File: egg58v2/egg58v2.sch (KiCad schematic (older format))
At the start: 32 parts, among them J1 AudioJack4, SW11 SW_PUSH_LED, SW12 SW_PUSH_LED, SW13 SW_PUSH_LED, SW14 SW_PUSH_LED, SW15 SW_PUSH_LED, SW16 SW_PUSH_LED, SW21 SW_PUSH_LED, SW22 SW_PUSH_LED, SW23 SW_PUSH_LED, SW24 SW_PUSH_LED, SW25 SW_PUSH_LED, SW26 SW_PUSH_LED, SW31 SW_PUSH_LED, SW32 SW_PUSH_LED, SW33 SW_PUSH_LED, SW34 SW_PUSH_LED, SW35 SW_PUSH_LED, SW36 SW_PUSH_LED, SW41 SW_PUSH_LED, SW42 SW_PUSH_LED, SW43 SW_PUSH_LED, SW44 SW_PUSH_LED, SW45 SW_PUSH_LED, SW46 SW_PUSH_LED, SW52 SW_PUSH_LED, SW53 SW_PUSH_LED, SW54 SW_PUSH_LED, SW55 SW_PUSH_LED, SW56 SW_PUSH_LED, U1 Elite-C

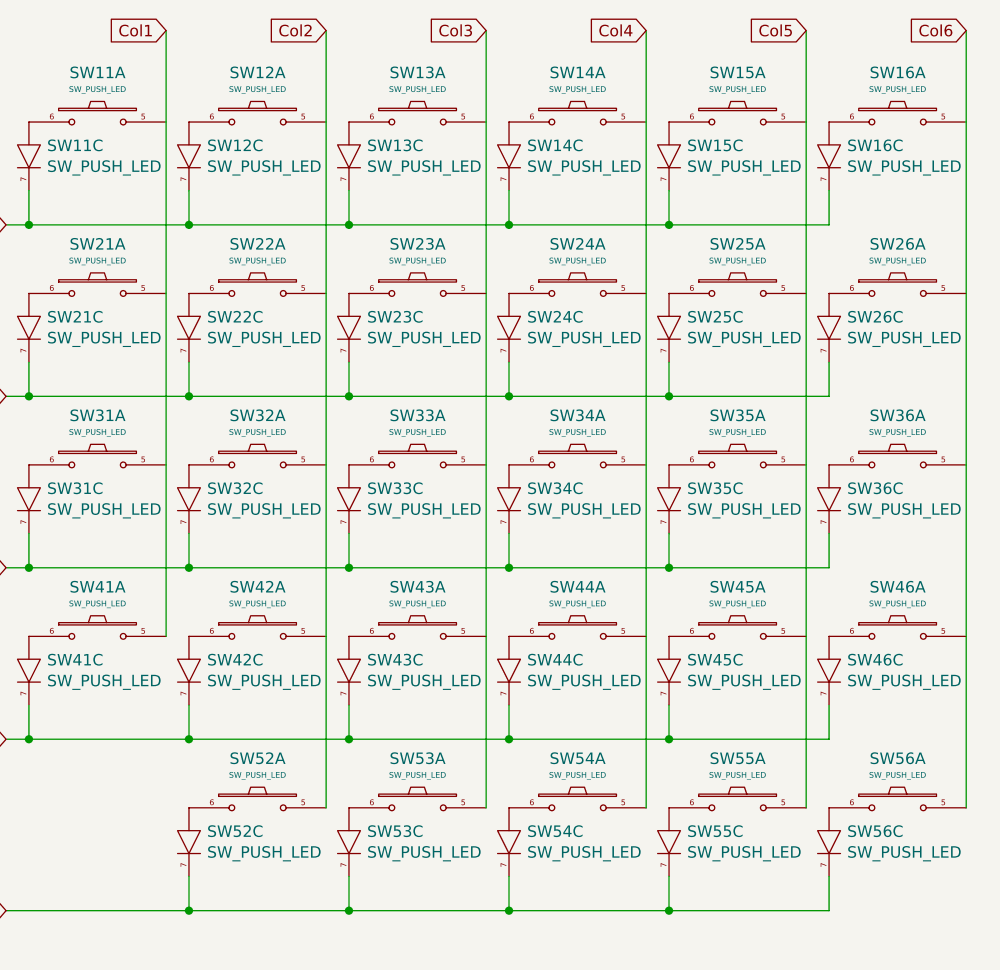
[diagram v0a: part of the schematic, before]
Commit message: footprint updates
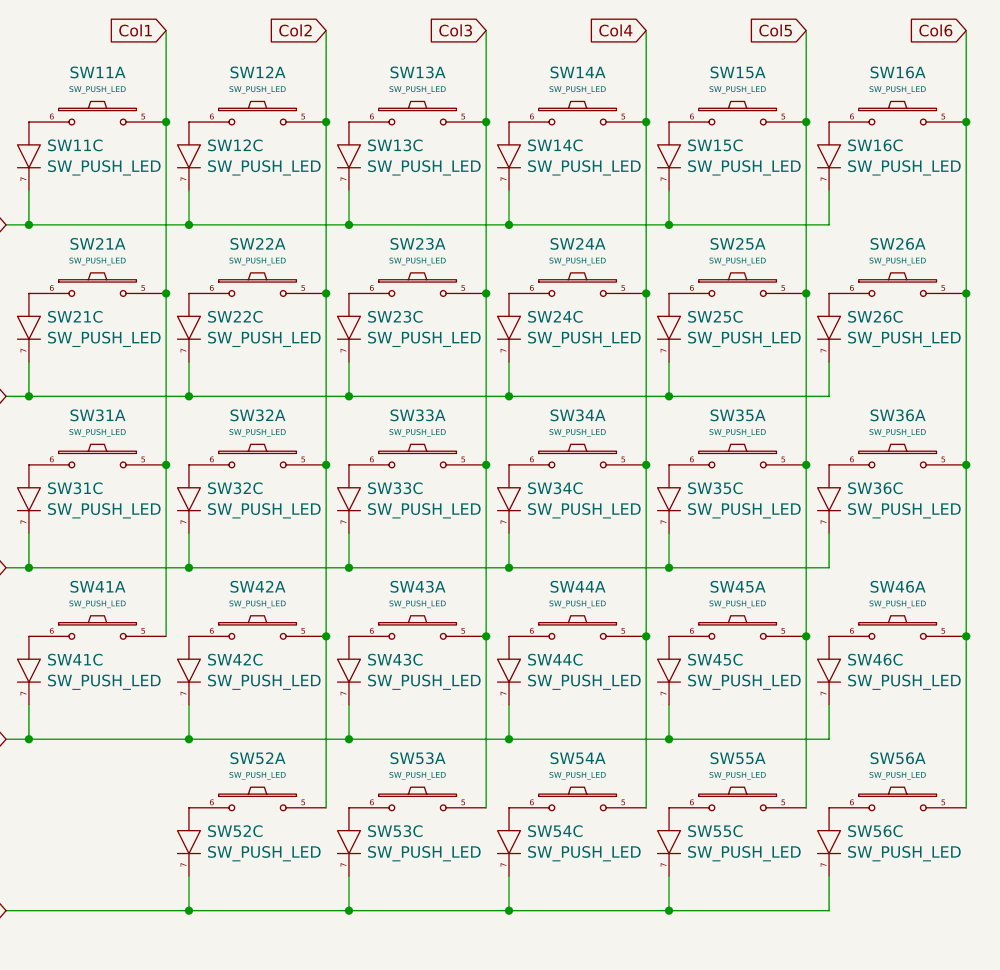
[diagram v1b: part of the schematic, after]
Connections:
- net Col1: now also SW11.5, SW21.5, SW31.5
- net Col2: now also SW12.5, SW22.5, SW32.5, SW42.5
- net Col3: now also SW13.5, SW23.5, SW33.5, SW43.5
- net Col4: now also SW14.5, SW24.5, SW34.5, SW44.5
- net Col5: now also SW15.5, SW25.5, SW35.5, SW45.5
- net Col6: now also SW16.5, SW26.5, SW36.5, SW46.5
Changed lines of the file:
@@
 	-1   0    0    1
 $EndComp
-Wire Wire Line
-	7550 650  7550 3300
-Wire Wire Line
-	8250 650  8250 4050
-Wire Wire Line
-	8950 650  8950 4050
-Wire Wire Line
-	9650 650  9650 4050
-Wire Wire Line
-	10350 650  10350 4050
-Wire Wire Line
-	11050 650  11050 4050
 Connection ~ 9750 3750
 Wire Wire Line
@@
 	1    0    0    -1
 $EndComp
+Wire Wire Line
+	7550 650  7550 1050
+Connection ~ 7550 1050
+Wire Wire Line
+	8250 650  8250 1050
+Connection ~ 8250 1050
+Wire Wire Line
+	8950 650  8950 1050
+Connection ~ 8950 1050
+Wire Wire Line
+	9650 650  9650 1050
+Connection ~ 9650 1050
+Wire Wire Line
+	10350 650  10350 1050
+Connection ~ 10350 1050
+Wire Wire Line
+	10350 1050 10350 1800
+Wire Wire Line
+	11050 650  11050 1050
+Connection ~ 11050 1050
+Wire Wire Line
+	11050 1050 11050 1800
+Connection ~ 11050 1800
+Wire Wire Line
+	11050 1800 11050 2550
+Connection ~ 10350 1800
+Wire Wire Line
+	10350 1800 10350 2550
+Connection ~ 11050 2550
+Wire Wire Line
+	11050 2550 11050 3300
+Connection ~ 10350 2550
+Wire Wire Line
+	10350 2550 10350 3300
+Connection ~ 11050 3300
+Wire Wire Line
+	11050 3300 11050 4050
+Connection ~ 10350 3300
+Wire Wire Line
+	10350 3300 10350 4050
+Wire Wire Line
+	9650 1050 9650 1800
+Connection ~ 9650 3300
+Wire Wire Line
+	9650 3300 9650 4050
+Connection ~ 9650 2550
+Wire Wire Line
+	9650 2550 9650 3300
+Wire Wire Line
+	9650 2550 9650 1800
+Connection ~ 9650 1800
+Wire Wire Line
+	8950 1050 8950 1800
+Connection ~ 8950 3300
+Wire Wire Line
+	8950 3300 8950 4050
+Connection ~ 8950 2550
+Wire Wire Line
+	8950 2550 8950 3300
+Wire Wire Line
+	8950 2550 8950 1800
+Connection ~ 8950 1800
+Wire Wire Line
+	8250 1050 8250 1800
+Connection ~ 8250 3300
+Wire Wire Line
+	8250 3300 8250 4050
+Connection ~ 8250 2550
+Wire Wire Line
+	8250 2550 8250 3300
+Wire Wire Line
+	8250 2550 8250 1800
+Connection ~ 8250 1800
+Wire Wire Line
+	7550 1050 7550 1800
+Connection ~ 7550 2550
+Wire Wire Line
+	7550 2550 7550 3300
+Connection ~ 7550 1800
+Wire Wire Line
+	7550 1800 7550 2550
 $EndSCHEMATC

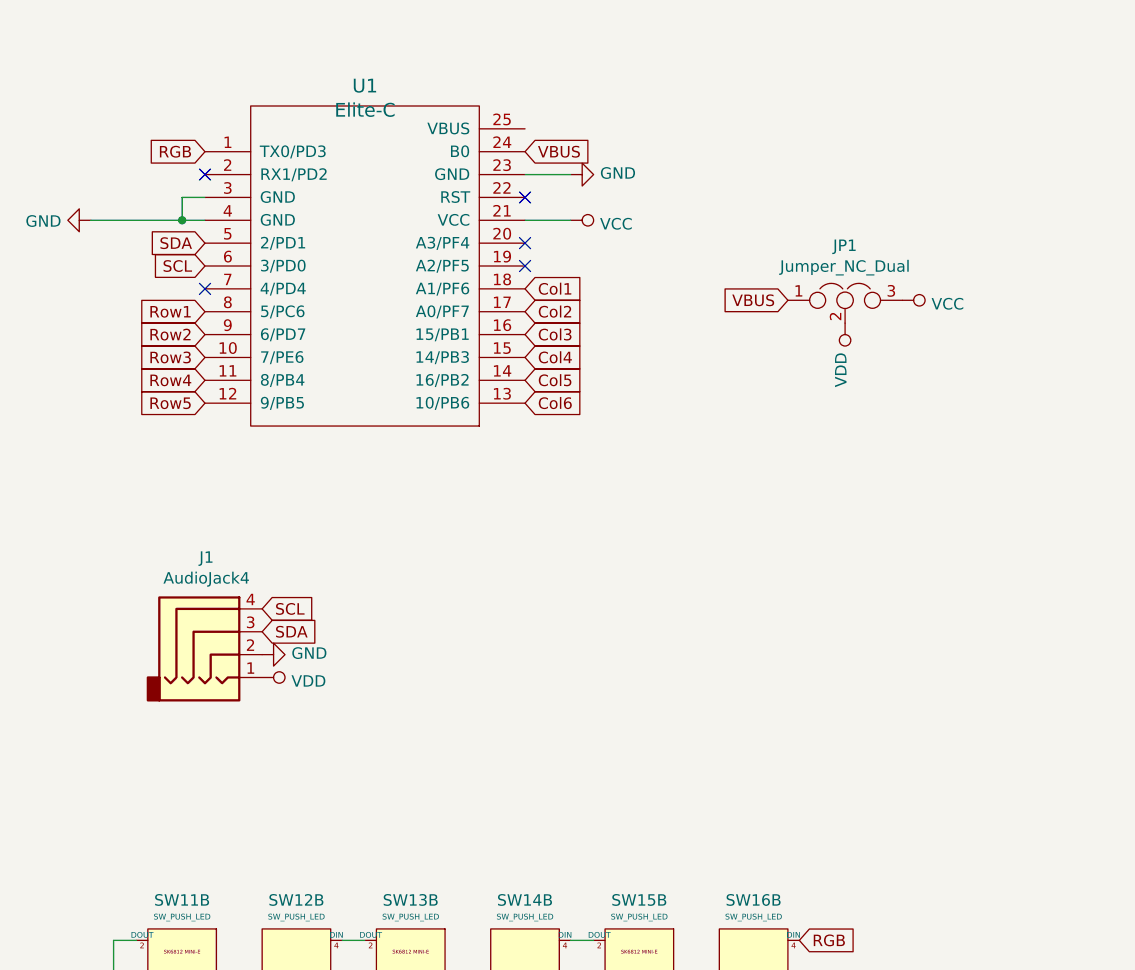
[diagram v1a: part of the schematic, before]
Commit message: add option for i2c back
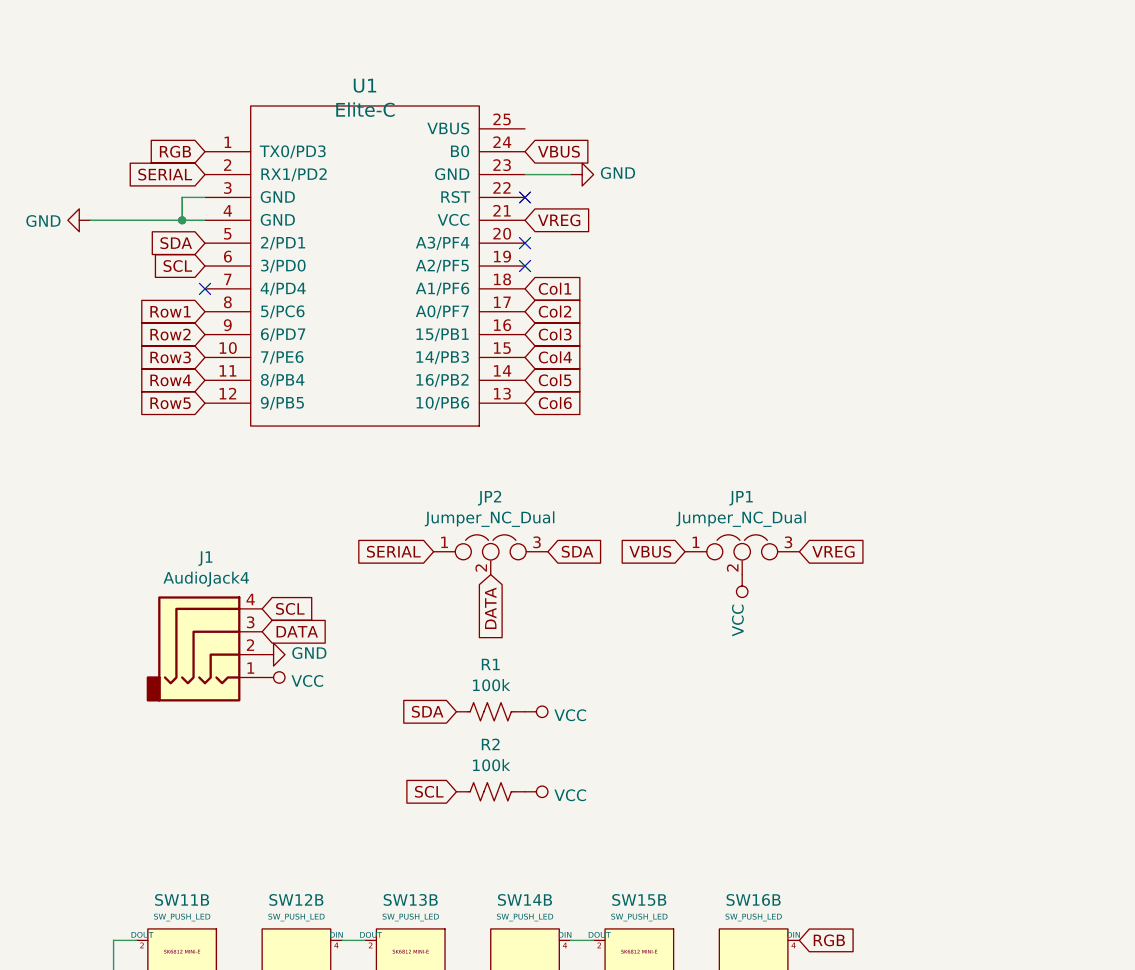
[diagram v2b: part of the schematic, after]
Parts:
- added JP2: Jumper_NC_Dual, egg58v2:SolderJumper-3_P1.3mm_Open_Pad1.0x1.5mm_NumberLabels, symbol Device:Jumper_NC_Dual
- added R1, R2: 100k, egg58v2:R_Axial_DIN0207_L6.3mm_D2.5mm_P10.16mm_Horizontal, symbol Device:R_US
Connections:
- net VDD is gone; now on net VCC: J1.1, JP1.2
- net SCL: now also R2.2
- net SDA: now also JP2.3, R1.2; no longer J1.3
- net VCC: now also R1.1, R2.1; no longer JP1.3, U1.21 (VCC)
- net SERIAL: now reaches U1.2 (RX1/PD2)
- net SERIAL: now also JP2.1
- new net DATA: J1.3, JP2.2
- new net VREG: JP1.3, U1.21 (VCC)
- no-connect marks 5 -> 4
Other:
- moved on the sheet: JP1
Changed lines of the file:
@@
 Connection ~ 9750 4500
-$Comp
-L egg58v2:Elite-C U1
-U 1 1 6215672D
-P 2000 1750
-F 0 "U1" H 2000 2587 60  0000 C CNN
-F 1 "Elite-C" H 2000 2481 60  0000 C CNN
-F 2 "egg58v2:ProMicro" V 3050 -750 60  0001 C CNN
-F 3 "" V 3050 -750 60  0001 C CNN
-	1    2000 1750
-	1    0    0    -1
-$EndComp
 $Comp
 L power:GND #PWR0101
@@
 	0    -1   -1   0
 $EndComp
-$Comp
-L power:VDD #PWR0104
-U 1 1 619C5956
-P 1550 3500
-F 0 "#PWR0104" H 1550 3350 50  0001 C CNN
-F 1 "VDD" V 1567 3628 50  0000 L CNN
-F 2 "" H 1550 3500 50  0001 C CNN
-F 3 "" H 1550 3500 50  0001 C CNN
-	1    1550 3500
-	0    1    1    0
-$EndComp
 Text GLabel 1300 1600 0    50   Input ~ 0
 SDA
@@
 NoConn ~ 2700 1600
 NoConn ~ 2700 1700
-NoConn ~ 1300 1300
 NoConn ~ 1300 1800
-Text GLabel 1550 3300 2    50   Input ~ 0
-SDA
 Text GLabel 1550 3200 2    50   Input ~ 0
 SCL
-Wire Wire Line
-	2900 1500 2700 1500
-$Comp
-L power:VCC #PWR0105
-U 1 1 61A2EFBB
-P 2900 1500
-F 0 "#PWR0105" H 2900 1350 50  0001 C CNN
-F 1 "VCC" V 2917 1628 50  0000 L CNN
-F 2 "" H 2900 1500 50  0001 C CNN
-F 3 "" H 2900 1500 50  0001 C CNN
-	1    2900 1500
-	0    1    1    0
-$EndComp
 Text GLabel 2700 1200 2    50   Input ~ 0
 VBUS
@@
 L Device:Jumper_NC_Dual JP1
 U 1 1 61A4B220
-P 4100 1850
-F 0 "JP1" H 4100 2089 50  0000 C CNN
-F 1 "Jumper_NC_Dual" H 4100 1998 50  0000 C CNN
-F 2 "egg58v2:SolderJumper-3_P1.3mm_Open_Pad1.0x1.5mm_NumberLabels" H 4100 1850 50  0001 C CNN
-F 3 "~" H 4100 1850 50  0001 C CNN
-	1    4100 1850
-	1    0    0    -1
-$EndComp
-Text GLabel 3850 1850 0    50   Input ~ 0
+P 3650 2950
+F 0 "JP1" H 3650 3189 50  0000 C CNN
+F 1 "Jumper_NC_Dual" H 3650 3098 50  0000 C CNN
+F 2 "egg58v2:SolderJumper-3_P1.3mm_Open_Pad1.0x1.5mm_NumberLabels" H 3650 2950 50  0001 C CNN
+F 3 "~" H 3650 2950 50  0001 C CNN
+	1    3650 2950
+	1    0    0    -1
+$EndComp
+Text GLabel 3400 2950 0    50   Input ~ 0
 VBUS
-$Comp
-L power:VCC #PWR0106
-U 1 1 61A4DE4C
-P 4350 1850
-F 0 "#PWR0106" H 4350 1700 50  0001 C CNN
-F 1 "VCC" V 4367 1978 50  0000 L CNN
-F 2 "" H 4350 1850 50  0001 C CNN
-F 3 "" H 4350 1850 50  0001 C CNN
-	1    4350 1850
-	0    1    1    0
-$EndComp
-$Comp
-L power:VDD #PWR0107
-U 1 1 61A4E8E6
-P 4100 1950
-F 0 "#PWR0107" H 4100 1800 50  0001 C CNN
-F 1 "VDD" V 4117 2078 50  0000 L CNN
-F 2 "" H 4100 1950 50  0001 C CNN
-F 3 "" H 4100 1950 50  0001 C CNN
-	1    4100 1950
-	-1   0    0    1
-$EndComp
 Connection ~ 9750 3750
 Wire Wire Line
@@
 Wire Wire Line
 	7550 1800 7550 2550
+$Comp
+L Device:Jumper_NC_Dual JP2
+U 1 1 61F3F4C1
+P 2550 2950
+F 0 "JP2" H 2550 3189 50  0000 C CNN
+F 1 "Jumper_NC_Dual" H 2550 3098 50  0000 C CNN
+F 2 "egg58v2:SolderJumper-3_P1.3mm_Open_Pad1.0x1.5mm_NumberLabels" H 2550 2950 50  0001 C CNN
+F 3 "~" H 2550 2950 50  0001 C CNN
+	1    2550 2950
+	1    0    0    -1
+$EndComp
+Text GLabel 1300 1300 0    50   Input ~ 0
+SERIAL
+Text GLabel 2300 2950 0    50   Input ~ 0
+SERIAL
+Text GLabel 2800 2950 2    50   Input ~ 0
+SDA
+$Comp
+L power:VCC #PWR0104
+U 1 1 61F625C6
+P 3650 3050
+F 0 "#PWR0104" H 3650 2900 50  0001 C CNN
+F 1 "VCC" V 3667 3178 50  0000 L CNN
+F 2 "" H 3650 3050 50  0001 C CNN
+F 3 "" H 3650 3050 50  0001 C CNN
+	1    3650 3050
+	-1   0    0    1
+$EndComp
+Text GLabel 3900 2950 2    50   Input ~ 0
+VREG
+Text GLabel 1550 3300 2    50   Input ~ 0
+DATA
+Text GLabel 2550 3050 3    50   Input ~ 0
+DATA
+Text GLabel 2400 3650 0    50   Input ~ 0
+SDA
+Text GLabel 2400 4000 0    50   Input ~ 0
+SCL
+$Comp
+L Device:R_US R2
+U 1 1 61F71586
+P 2550 4000
+F 0 "R2" V 2345 4000 50  0000 C CNN
+F 1 "100k" V 2436 4000 50  0000 C CNN
+F 2 "egg58v2:R_Axial_DIN0207_L6.3mm_D2.5mm_P10.16mm_Horizontal" V 2590 3990 50  0001 C CNN
+F 3 "~" H 2550 4000 50  0001 C CNN
+	1    2550 4000
+	0    1    1    0
+$EndComp
+$Comp
+L Device:R_US R1
+U 1 1 61F71DFC
+P 2550 3650
+F 0 "R1" V 2345 3650 50  0000 C CNN
+F 1 "100k" V 2436 3650 50  0000 C CNN
+F 2 "egg58v2:R_Axial_DIN0207_L6.3mm_D2.5mm_P10.16mm_Horizontal" V 2590 3640 50  0001 C CNN
+F 3 "~" H 2550 3650 50  0001 C CNN
+	1    2550 3650
+	0    1    1    0
+$EndComp
+$Comp
+L power:VCC #PWR0105
+U 1 1 61F83E20
+P 2700 3650
+F 0 "#PWR0105" H 2700 3500 50  0001 C CNN
+F 1 "VCC" V 2717 3778 50  0000 L CNN
+F 2 "" H 2700 3650 50  0001 C CNN
+F 3 "" H 2700 3650 50  0001 C CNN
+	1    2700 3650
+	0    1    1    0
+$EndComp
+$Comp
+L power:VCC #PWR0106
+U 1 1 61F8A8DD
+P 2700 4000
+F 0 "#PWR0106" H 2700 3850 50  0001 C CNN
+F 1 "VCC" V 2717 4128 50  0000 L CNN
+F 2 "" H 2700 4000 50  0001 C CNN
+F 3 "" H 2700 4000 50  0001 C CNN
+	1    2700 4000
+	0    1    1    0
+$EndComp
+$Comp
+L power:VCC #PWR0107
+U 1 1 61F97A9B
+P 1550 3500
+F 0 "#PWR0107" H 1550 3350 50  0001 C CNN
+F 1 "VCC" V 1567 3628 50  0000 L CNN
+F 2 "" H 1550 3500 50  0001 C CNN
+F 3 "" H 1550 3500 50  0001 C CNN
+	1    1550 3500
+	0    1    1    0
+$EndComp
+Text GLabel 2700 1500 2    50   Input ~ 0
+VREG
+$Comp
+L egg58v2:Elite-C U1
+U 1 1 6215672D
+P 2000 1750
+F 0 "U1" H 2000 2587 60  0000 C CNN
+F 1 "Elite-C" H 2000 2481 60  0000 C CNN
+F 2 "egg58v2:ProMicro" V 3050 -750 60  0001 C CNN
+F 3 "" V 3050 -750 60  0001 C CNN
+	1    2000 1750
+	1    0    0    -1
+$EndComp
 $EndSCHEMATC

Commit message: starting routing
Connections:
- no-connect marks 4 -> 5
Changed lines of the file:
@@
 F 1 "SW_PUSH_LED" V 10405 1121 50  0000 R CNN
 F 2 "egg58v2:Choc_Hotswap_SK6812MiniE" H 10450 1200 50  0001 C CNN
-F 3 "~" H 10450 1200 50  0001 C CNN
+F 3 "" H 10450 1200 50  0001 C CNN
 	3    10450 1200
 	0    -1   -1   0
@@
 	1    0    0    -1
 $EndComp
+NoConn ~ 1500 6850
 $EndSCHEMATC

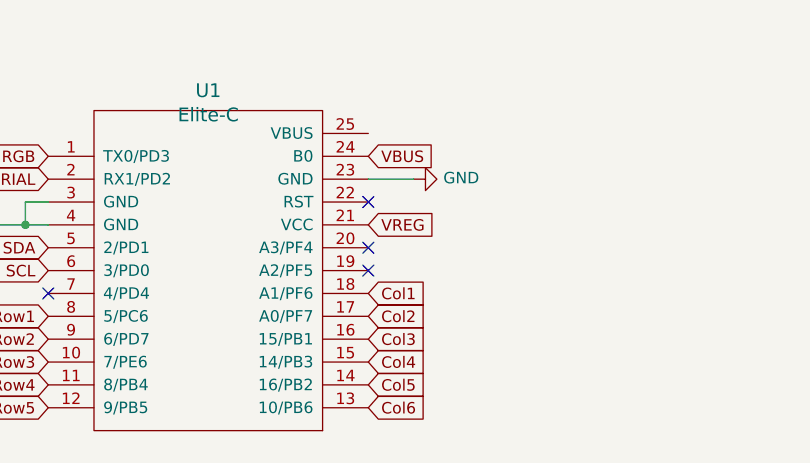
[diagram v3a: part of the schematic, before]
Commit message: Add support for VBUS from EliteC
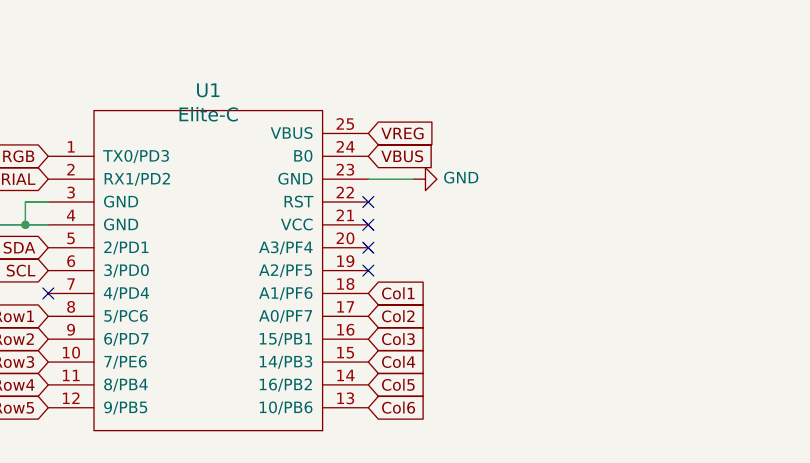
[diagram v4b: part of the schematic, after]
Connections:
- net VREG: now also U1.25 (VBUS); no longer U1.21 (VCC)
- no-connect marks 5 -> 6
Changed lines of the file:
@@
 Sheet 1 1
 Title "egg58"
-Date "2022-01-23"
-Rev "2"
+Date "2022-06-28"
+Rev "2.1"
 Comp ""
 Comment1 "github.com/tmick0/egg58"
 Comment2 "a sanely minimalist split keyboard"
-Comment3 "egg58v2"
+Comment3 "egg58v2.1"
 Comment4 ""
 $EndDescr
@@
 	0    1    1    0
 $EndComp
-Text GLabel 2700 1500 2    50   Input ~ 0
+Text GLabel 2700 1100 2    50   Input ~ 0
 VREG
 $Comp
@@
 $EndComp
 NoConn ~ 1500 6850
+NoConn ~ 2700 1500
 $EndSCHEMATC
